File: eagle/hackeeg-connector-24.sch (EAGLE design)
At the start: 49 parts

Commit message: updated libraries to current
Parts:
- AGND, AGND1, AGND2, IN1P-1, IN1P-17, IN1P-9, IN2P-10, IN2P-18, IN2P-2, IN3P-11, IN3P-19, IN3P-3, IN4P-12, IN4P-20, IN4P-4, IN5N-22, IN5P-13, IN5P-21, IN5P-5, IN6N-24, IN6P-14, IN6P-23, IN6P-6, IN7N-26, IN7P-15, IN7P-25, IN7P-7, IN8N-28, IN8P-16, IN8P-27, IN8P-8: value PO37729HEX-100 -> PO37729HEX-110; device po-37729:PO37729HEX-100 -> po-37729:PO37729HEX-110
- ELECTRODE-CONNECTOR, ELECTRODE-CONNECTOR1, ELECTRODE-CONNECTOR2: value SBH11-NBPC-D12-SM-BKJ -> SBH11-NBPC-D12-SM-BK; device SBH11-NBPC-D12-SM-BK:SBH11-NBPC-D12-SM-BKJ -> SBH11-NBPC-D12-SM-BK:SBH11-NBPC-D12-SM-BK
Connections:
- removed net N$1: AGND.SIGNAL, ELECTRODE-CONNECTOR.5
- removed net N$10: AGND1.SIGNAL, ELECTRODE-CONNECTOR1.5
- removed net N$19: AGND2.SIGNAL, ELECTRODE-CONNECTOR2.5
- new net AGND: AGND.SIGNAL, AGND1.SIGNAL, AGND2.SIGNAL, ELECTRODE-CONNECTOR.10, ELECTRODE-CONNECTOR.12, ELECTRODE-CONNECTOR.14, ELECTRODE-CONNECTOR.16, ELECTRODE-CONNECTOR.18, ELECTRODE-CONNECTOR.20, ELECTRODE-CONNECTOR.22, ELECTRODE-CONNECTOR.4, ELECTRODE-CONNECTOR.5, ELECTRODE-CONNECTOR.6, ELECTRODE-CONNECTOR.8, ELECTRODE-CONNECTOR1.10, ELECTRODE-CONNECTOR1.12, ELECTRODE-CONNECTOR1.14, ELECTRODE-CONNECTOR1.16, ELECTRODE-CONNECTOR1.18, ELECTRODE-CONNECTOR1.20, ELECTRODE-CONNECTOR1.22, ELECTRODE-CONNECTOR1.4, ELECTRODE-CONNECTOR1.5, ELECTRODE-CONNECTOR1.6, ELECTRODE-CONNECTOR1.8, ELECTRODE-CONNECTOR2.10, ELECTRODE-CONNECTOR2.12, ELECTRODE-CONNECTOR2.14, ELECTRODE-CONNECTOR2.4, ELECTRODE-CONNECTOR2.5, ELECTRODE-CONNECTOR2.6, ELECTRODE-CONNECTOR2.8

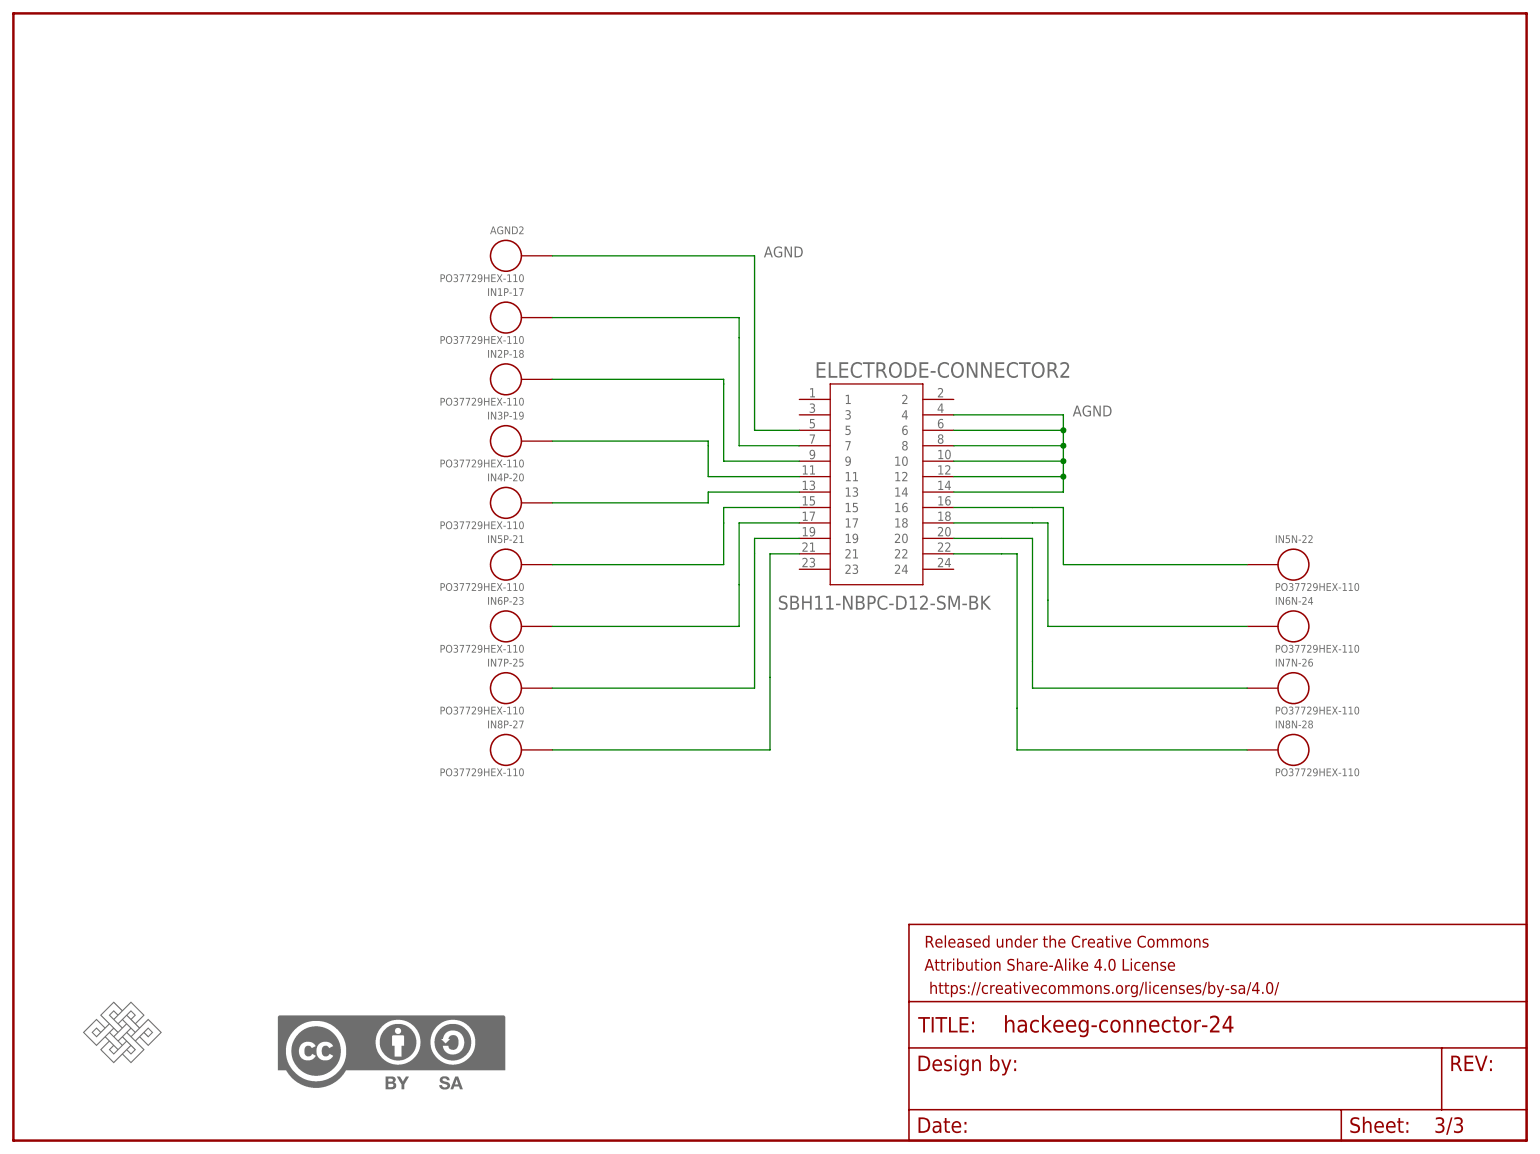
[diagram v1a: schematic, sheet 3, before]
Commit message: relicense to CERN OHL 1.2 - sch
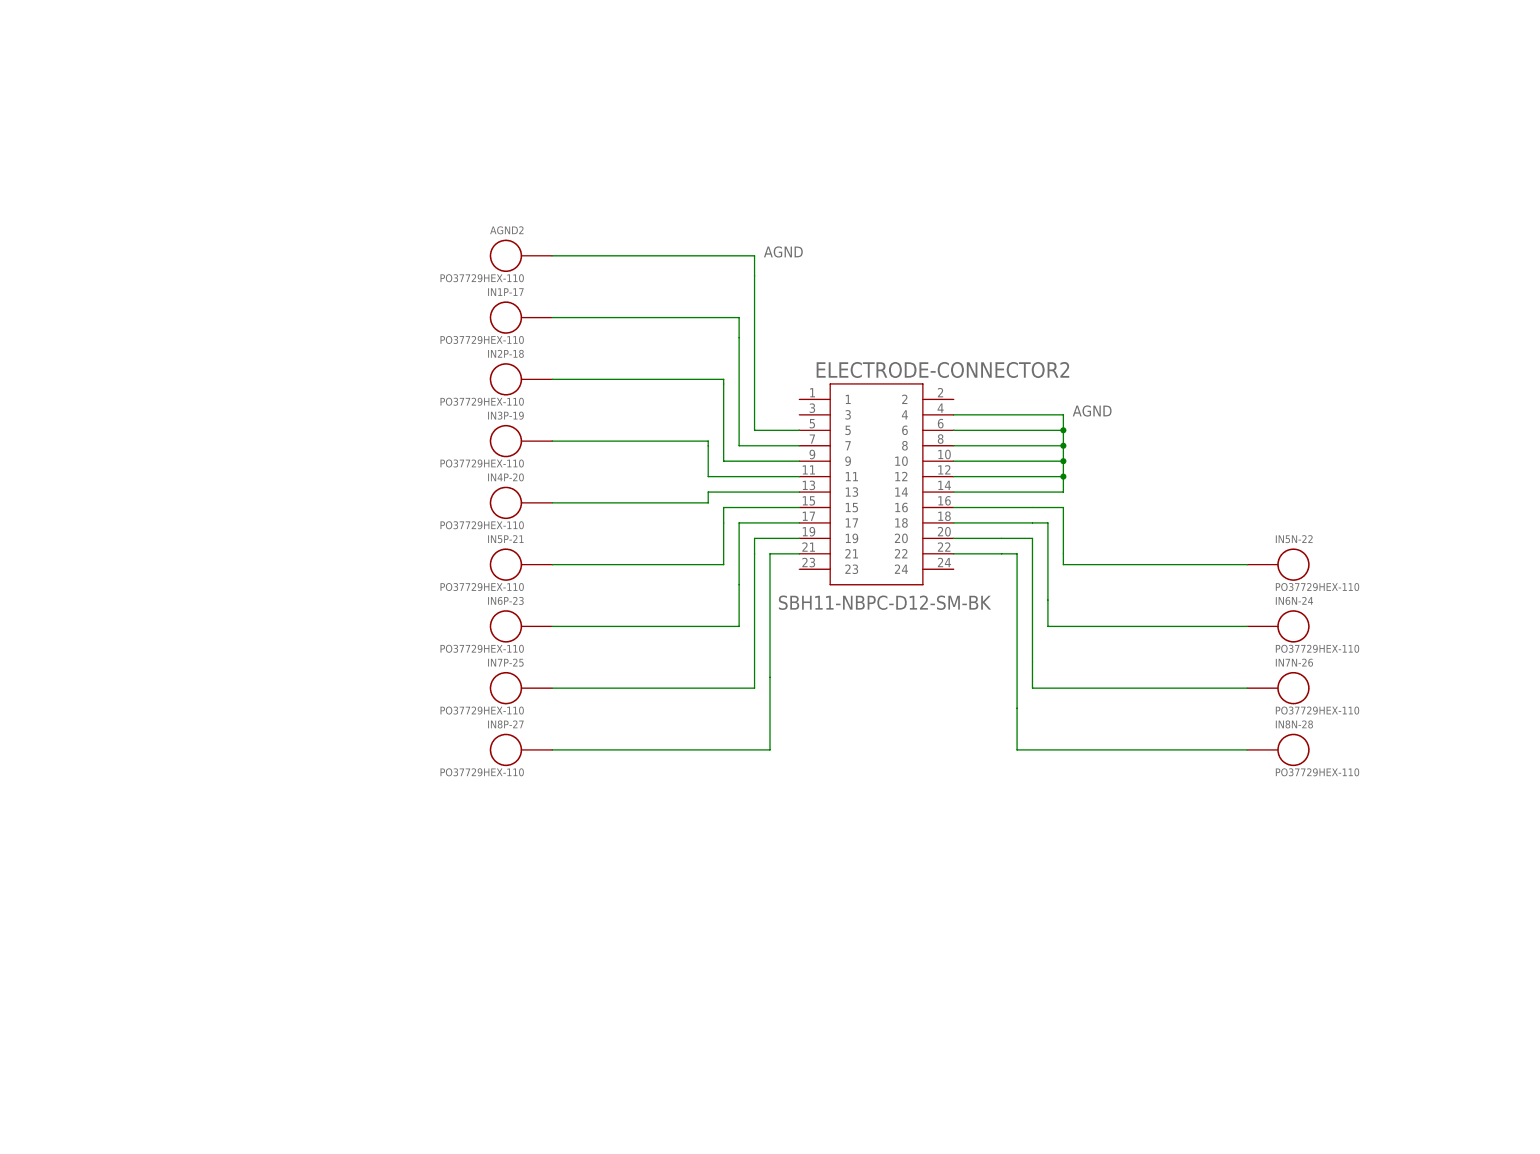
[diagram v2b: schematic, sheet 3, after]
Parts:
- removed FRAME1, FRAME2, FRAME3: FRAME-LETTER, SparkFun-Aesthetics:FRAME-LETTER
- removed U$13, U$2, U$4: CC-BY-SA, creative-commons:CC-BY-SA
- removed U$3, U$5: ENDLESSKNOTENDLESSKNOT-MEDIUM, endless-knot:ENDLESSKNOTENDLESSKNOT-MEDIUM
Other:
- note added: "v0.2"
- note added: "© 2019 Adam Feuer Released under the CERN Open Hardware License v.1.2"
